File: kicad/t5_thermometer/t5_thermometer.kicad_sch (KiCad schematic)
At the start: 17 parts, among them J1 DBG, J3 Display, U1 STM32F042F6Px, U2 TSR_1-2433

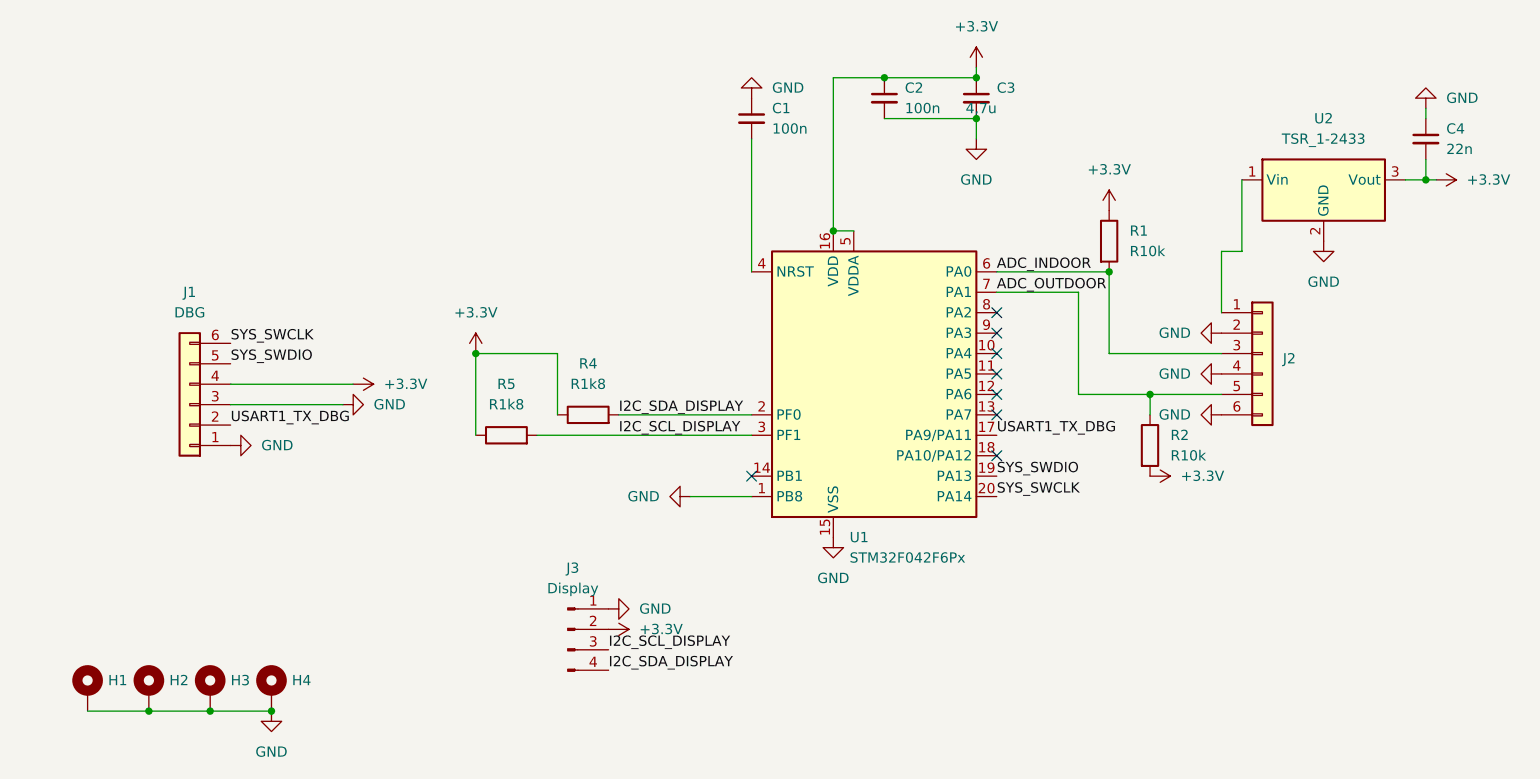
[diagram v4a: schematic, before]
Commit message: Change Layout to match the current working status: BOOT0 is now connected to GND
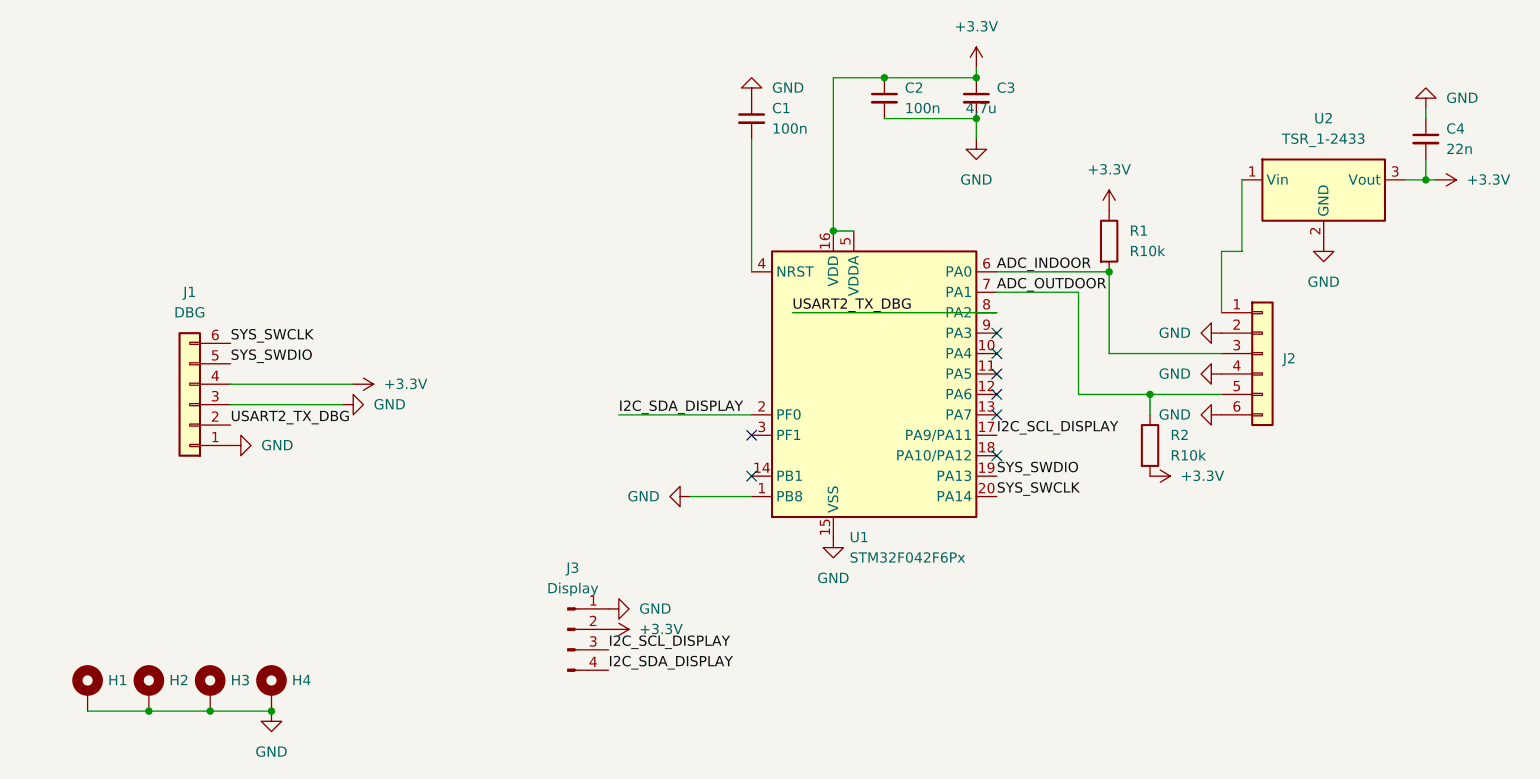
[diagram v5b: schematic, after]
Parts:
- removed R4, R5: R1k8, Resistor_SMD:R_0603_1608Metric_Pad0.98x0.95mm_HandSolder, symbol Device:R
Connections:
- net I2C_SCL_DISPLAY: now also U1.17 (PA9/PA11); no longer U1.3 (PF1)
- net USART2_TX_DBG: now reaches U1.8 (PA2)
- net USART2_TX_DBG: now also J1.2 (Pin_2)
- removed net USART1_TX_DBG: J1.2 (Pin_2), U1.17 (PA9/PA11)
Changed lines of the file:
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@@
-	)
-	(junction
-		(at 133.35 88.9)
-		(diameter 0)
-		(color 0 0 0 0)
 	)
 	(junction
@@
 	)
 	(no_connect
+		(at 167.64 99.06)
+	)
+	(no_connect
 		(at 198.12 93.98)
 	)
@@
 	)
 	(no_connect
-		(at 198.12 83.82)
-	)
-	(no_connect
 		(at 198.12 91.44)
 	)
@@
 	(wire
 		(pts
-			(xy 143.51 88.9) (xy 143.51 96.52)
-		)
-		(stroke
-			(width 0)
-			(type default)
-		)
-	)
-	(wire
-		(pts
 			(xy 177.8 73.66) (xy 180.34 73.66)
 		)
@@
 	(wire
 		(pts
+			(xy 172.72 83.82) (xy 198.12 83.82)
+		)
+		(stroke
+			(width 0)
+			(type default)
+		)
+	)
+	(wire
+		(pts
 			(xy 252.73 67.31) (xy 251.46 67.31)
 		)
@@
 	(wire
 		(pts
-			(xy 133.35 99.06) (xy 133.35 88.9)
-		)
-		(stroke
-			(width 0)
-			(type default)
-		)
-	)
-	(wire
-		(pts
 			(xy 228.6 67.31) (xy 228.6 76.2)
 		)
@@
 	(wire
 		(pts
-			(xy 140.97 99.06) (xy 167.64 99.06)
-		)
-		(stroke
-			(width 0)
-			(type default)
-		)
-	)
-	(wire
-		(pts
 			(xy 251.46 58.42) (xy 251.46 59.69)
 		)
@@
 		(pts
 			(xy 208.28 81.28) (xy 198.12 81.28)
-		)
-		(stroke
-			(width 0)
-			(type default)
-		)
-	)
-	(wire
-		(pts
-			(xy 133.35 88.9) (xy 143.51 88.9)
 		)
 		(stroke
@@
 		)
 	)
-	(label "USART1_TX_DBG"
-		(at 198.12 99.06 0)
+	(label "USART2_TX_DBG"
+		(at 172.72 83.82 0)
 		(fields_autoplaced yes)
 		(effects
@@
 		)
 	)
-	(label "USART1_TX_DBG"
-		(at 102.87 97.79 0)
+	(label "I2C_SCL_DISPLAY"
+		(at 198.12 99.06 0)
 		(fields_autoplaced yes)
 		(effects
@@
 		)
 	)
-	(label "I2C_SDA_DISPLAY"
-		(at 151.13 96.52 0)
+	(label "USART2_TX_DBG"
+		(at 102.87 97.79 0)
 		(fields_autoplaced yes)
 		(effects
@@
 		)
 	)
-	(label "I2C_SCL_DISPLAY"
-		(at 151.13 99.06 0)
+	(label "I2C_SDA_DISPLAY"
+		(at 151.13 96.52 0)
 		(fields_autoplaced yes)
 		(effects
@@
 		(on_board yes)
 		(dnp no)
-		(fields_autoplaced yes)
 		(property "Reference" "U1"
 			(at 179.8194 111.76 0)
@@
 	)
 	(symbol
-		(lib_id "power:+3.3V")
-		(at 133.35 88.9 0)
-		(unit 1)
-		(exclude_from_sim no)
-		(in_bom yes)
-		(on_board yes)
-		(dnp no)
-		(fields_autoplaced yes)
-		(property "Reference" "#PWR020"
-			(at 133.35 92.71 0)
-			(effects
-				(font
-					(size 1.27 1.27)
-				)
-				(hide yes)
-			)
-		)
-		(property "Value" "+3.3V"
-			(at 133.35 83.82 0)
-			(effects
-				(font
-					(size 1.27 1.27)
-				)
-			)
-		)
-		(property "Footprint" ""
-			(at 133.35 88.9 0)
-			(effects
-				(font
-					(size 1.27 1.27)
-				)
-				(hide yes)
-			)
-		)
-		(property "Datasheet" ""
-			(at 133.35 88.9 0)
-			(effects
-				(font
-					(size 1.27 1.27)
-				)
-				(hide yes)
-			)
-		)
-		(property "Description" ""
-			(at 133.35 88.9 0)
-			(effects
-				(font
-					(size 1.27 1.27)
-				)
-				(hide yes)
-			)
-		)
-		(pin "1"
-		)
-		(instances
-			(project "t5_thermometer"
-				(path "/50047928-ac31-4fdc-a3a3-efe1c714e937"
-					(reference "#PWR020")
-					(unit 1)
-				)
-			)
-		)
-	)
-	(symbol
-		(lib_id "Device:R")
-		(at 137.16 99.06 90)
-		(unit 1)
-		(exclude_from_sim no)
-		(in_bom yes)
-		(on_board yes)
-		(dnp no)
-		(fields_autoplaced yes)
-		(property "Reference" "R5"
-			(at 137.16 92.71 90)
-			(effects
-				(font
-					(size 1.27 1.27)
-				)
-			)
-		)
-		(property "Value" "R1k8"
-			(at 137.16 95.25 90)
-			(effects
-				(font
-					(size 1.27 1.27)
-				)
-			)
-		)
-		(property "Footprint" "Resistor_SMD:R_0603_1608Metric_Pad0.98x0.95mm_HandSolder"
-			(at 137.16 100.838 90)
-			(effects
-				(font
-					(size 1.27 1.27)
-				)
-				(hide yes)
-			)
-		)
-		(property "Datasheet" "~"
-			(at 137.16 99.06 0)
-			(effects
-				(font
-					(size 1.27 1.27)
-				)
-				(hide yes)
-			)
-		)
-		(property "Description" "Resistor"
-			(at 137.16 99.06 0)
-			(effects
-				(font
-					(size 1.27 1.27)
-				)
-				(hide yes)
-			)
-		)
-		(pin "1"
-		)
-		(pin "2"
-		)
-		(instances
-			(project "t5_thermometer"
-				(path "/50047928-ac31-4fdc-a3a3-efe1c714e937"
-					(reference "R5")
-					(unit 1)
-				)
-			)
-		)
-	)
-	(symbol
 		(lib_id "Device:R")
 		(at 217.17 100.33 0)
@@
 					(unit 1)
 				)
-			)
-		)
-	)
-	(symbol
-		(lib_id "Device:R")
-		(at 147.32 96.52 90)
-		(unit 1)
-		(exclude_from_sim no)
-		(in_bom yes)
-		(on_board yes)
-		(dnp no)
-		(fields_autoplaced yes)
-		(property "Reference" "R4"
-			(at 147.32 90.17 90)
-			(effects
-				(font
-					(size 1.27 1.27)
-				)
-			)
-		)
-		(property "Value" "R1k8"
-			(at 147.32 92.71 90)
-			(effects
-				(font
-					(size 1.27 1.27)
-				)
-			)
-		)
-		(property "Footprint" "Resistor_SMD:R_0603_1608Metric_Pad0.98x0.95mm_HandSolder"
-			(at 147.32 98.298 90)
-			(effects
-				(font
-					(size 1.27 1.27)
-				)
-				(hide yes)
-			)
-		)
-		(property "Datasheet" "~"
-			(at 147.32 96.52 0)
-			(effects
-				(font
-					(size 1.27 1.27)
-				)
-				(hide yes)
-			)
-		)
-		(property "Description" "Resistor"
-			(at 147.32 96.52 0)
-			(effects
-				(font
-					(size 1.27 1.27)
-				)
-				(hide yes)
-			)
-		)
-		(pin "1"
-		)
-		(pin "2"
-		)
-		(instances
-			(project "t5_thermometer"
-				(path "/50047928-ac31-4fdc-a3a3-efe1c714e937"
-					(reference "R4")
-					(unit 1)
-				)
